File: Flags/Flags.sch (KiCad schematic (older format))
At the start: 22 parts, among them J1 Conn_01x07_Male, J2 Conn_01x06_Male, J3 Conn_01x03_Male, J4 Conn_01x04_Male, U1 74LS08, U2 74HC74, U3 74LS175

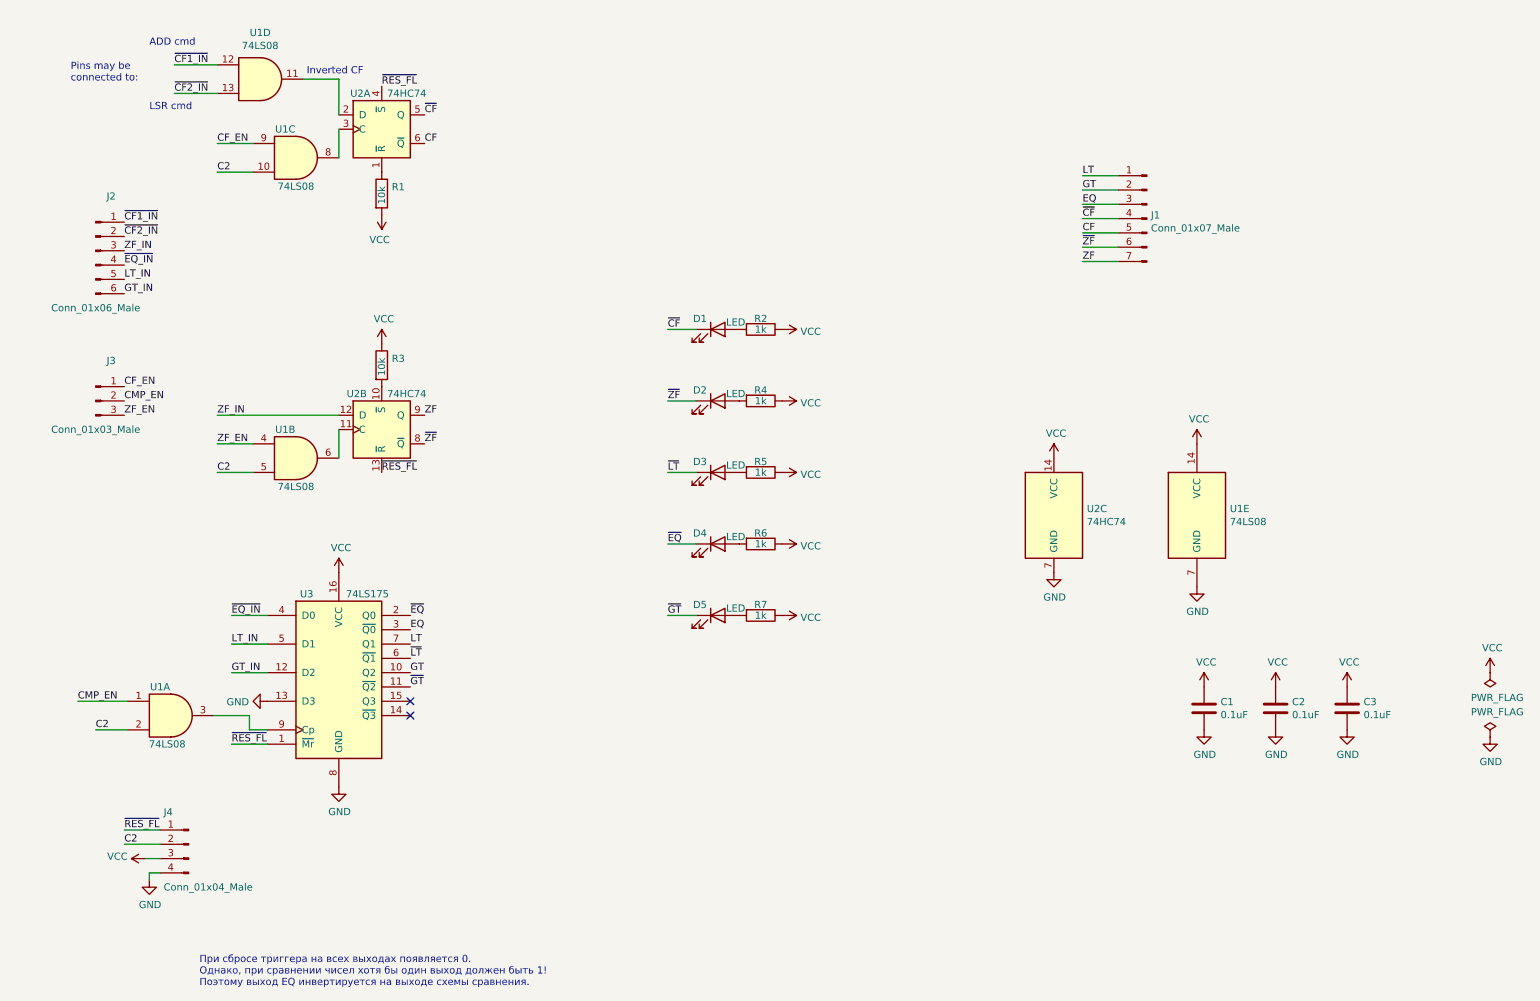
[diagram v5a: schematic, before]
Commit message: Polishing Flags. Add lost pins.
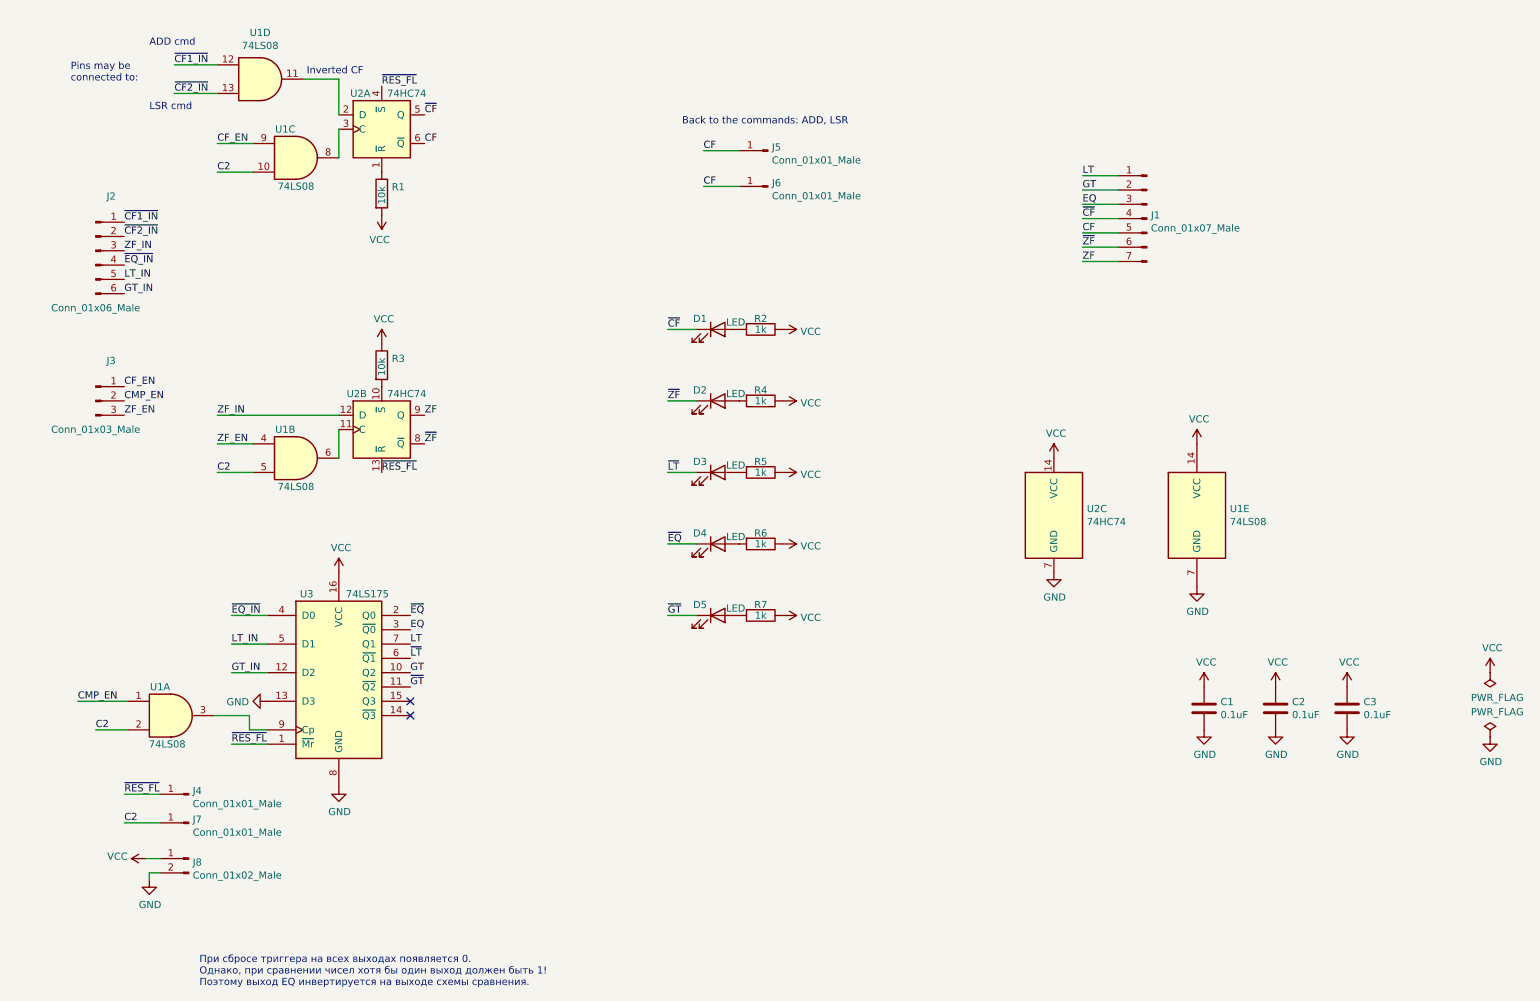
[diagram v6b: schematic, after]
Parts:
- removed J4: Conn_01x04_Male, Connector_PinHeader_2.54mm:PinHeader_1x04_P2.54mm_Vertical, symbol Connector:Conn_01x04_Male
- added J4, J5, J6, J7: Conn_01x01_Male, Connector_PinHeader_2.54mm:PinHeader_1x01_P2.54mm_Vertical, symbol Connector:Conn_01x01_Male
- added J8: Conn_01x02_Male, Connector_PinHeader_2.54mm:PinHeader_1x02_P2.54mm_Vertical, symbol Connector:Conn_01x02_Male
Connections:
- net C2: now also J7.1 (Pin_1)
- net CF: now also J5.1 (Pin_1), J6.1 (Pin_1)
- net GND: now also J8.2 (Pin_2)
- net VCC: now also J8.1 (Pin_1)
- net ~RES_FL: now also J4.1 (Pin_1)
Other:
- note added: "Back to the commands: ADD, LSR"
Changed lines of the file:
@@
 Text Label 7900 2525 0    50   ~ 0
 ZF
-$Comp
-L Connector:Conn_01x04_Male J4
-U 1 1 62C55960
-P 1650 6600
-F 0 "J4" H 1825 6825 50  0000 R CNN
-F 1 "Conn_01x04_Male" H 1825 6300 50  0000 R CNN
-F 2 "Connector_PinHeader_2.54mm:PinHeader_1x04_P2.54mm_Vertical" H 1650 6600 50  0001 C CNN
-F 3 "~" H 1650 6600 50  0001 C CNN
-	1    1650 6600
-	-1   0    0    -1
-$EndComp
-Wire Wire Line
-	1200 6500 1450 6500
-Wire Wire Line
-	1200 6600 1450 6600
-Text Label 1200 6600 0    50   ~ 0
+Wire Wire Line
+	1200 6250 1450 6250
+Wire Wire Line
+	1200 6450 1450 6450
+Text Label 1200 6450 0    50   ~ 0
 C2
-Text Label 1200 6500 0    50   ~ 0
+Text Label 1200 6250 0    50   ~ 0
 ~RES_FL
 $Comp
@@
 	-1   0    0    -1
 $EndComp
+$Comp
+L Connector:Conn_01x01_Male J5
+U 1 1 63FB964B
+P 5700 1750
+F 0 "J5" H 5672 1774 50  0000 R CNN
+F 1 "Conn_01x01_Male" H 5672 1683 50  0000 R CNN
+F 2 "Connector_PinHeader_2.54mm:PinHeader_1x01_P2.54mm_Vertical" H 5700 1750 50  0001 C CNN
+F 3 "~" H 5700 1750 50  0001 C CNN
+	1    5700 1750
+	-1   0    0    -1
+$EndComp
+$Comp
+L Connector:Conn_01x01_Male J6
+U 1 1 63FBB2B0
+P 5700 2000
+F 0 "J6" H 5672 2024 50  0000 R CNN
+F 1 "Conn_01x01_Male" H 5672 1933 50  0000 R CNN
+F 2 "Connector_PinHeader_2.54mm:PinHeader_1x01_P2.54mm_Vertical" H 5700 2000 50  0001 C CNN
+F 3 "~" H 5700 2000 50  0001 C CNN
+	1    5700 2000
+	-1   0    0    -1
+$EndComp
+Wire Wire Line
+	5250 1750 5500 1750
+Wire Wire Line
+	5250 2000 5500 2000
+Text Label 5250 1750 0    50   ~ 0
+CF
+Text Label 5250 2000 0    50   ~ 0
+CF
+Text Notes 5100 1575 0    50   ~ 0
+Back to the commands: ADD, LSR
+$Comp
+L Connector:Conn_01x02_Male J8
+U 1 1 640113A9
+P 1650 6700
+F 0 "J8" H 1622 6674 50  0000 R CNN
+F 1 "Conn_01x02_Male" H 1622 6583 50  0000 R CNN
+F 2 "Connector_PinHeader_2.54mm:PinHeader_1x02_P2.54mm_Vertical" H 1650 6700 50  0001 C CNN
+F 3 "~" H 1650 6700 50  0001 C CNN
+	1    1650 6700
+	-1   0    0    -1
+$EndComp
+$Comp
+L Connector:Conn_01x01_Male J4
+U 1 1 64013AFE
+P 1650 6250
+F 0 "J4" H 1622 6274 50  0000 R CNN
+F 1 "Conn_01x01_Male" H 1622 6183 50  0000 R CNN
+F 2 "Connector_PinHeader_2.54mm:PinHeader_1x01_P2.54mm_Vertical" H 1650 6250 50  0001 C CNN
+F 3 "~" H 1650 6250 50  0001 C CNN
+	1    1650 6250
+	-1   0    0    -1
+$EndComp
+$Comp
+L Connector:Conn_01x01_Male J7
+U 1 1 6401693F
+P 1650 6450
+F 0 "J7" H 1622 6474 50  0000 R CNN
+F 1 "Conn_01x01_Male" H 1622 6383 50  0000 R CNN
+F 2 "Connector_PinHeader_2.54mm:PinHeader_1x01_P2.54mm_Vertical" H 1650 6450 50  0001 C CNN
+F 3 "~" H 1650 6450 50  0001 C CNN
+	1    1650 6450
+	-1   0    0    -1
+$EndComp

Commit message: Polishing Flags. Add mounting holes.
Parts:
- added H1, H2: MountingHole, MountingHole:MountingHole_3.2mm_M3, symbol Mechanical:MountingHole
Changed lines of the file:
@@
 	-1   0    0    -1
 $EndComp
+$Comp
+L Mechanical:MountingHole H1
+U 1 1 64692F19
+P 7500 5500
+F 0 "H1" H 7600 5546 50  0000 L CNN
+F 1 "MountingHole" H 7600 5455 50  0000 L CNN
+F 2 "MountingHole:MountingHole_3.2mm_M3" H 7500 5500 50  0001 C CNN
+F 3 "~" H 7500 5500 50  0001 C CNN
+	1    7500 5500
+	1    0    0    -1
+$EndComp
+$Comp
+L Mechanical:MountingHole H2
+U 1 1 64693311
+P 7500 5750
+F 0 "H2" H 7600 5796 50  0000 L CNN
+F 1 "MountingHole" H 7600 5705 50  0000 L CNN
+F 2 "MountingHole:MountingHole_3.2mm_M3" H 7500 5750 50  0001 C CNN
+F 3 "~" H 7500 5750 50  0001 C CNN
+	1    7500 5750
+	1    0    0    -1
+$EndComp
 $EndSCHEMATC

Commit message: Polishing Flags
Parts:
- added H3, H4: MountingHole, MountingHole:MountingHole_3.2mm_M3, symbol Mechanical:MountingHole
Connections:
- net CMP_EN: now also J3.3 (Pin_3); no longer J3.2 (Pin_2)
- net ZF_EN: now also J3.2 (Pin_2); no longer J3.3 (Pin_3)
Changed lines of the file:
@@
 Text Label 1200 2450 0    50   ~ 0
 ZF_IN
+Text Label 1200 3500 0    50   ~ 0
+ZF_EN
 Text Label 1200 3600 0    50   ~ 0
-ZF_EN
-Text Label 1200 3500 0    50   ~ 0
 CMP_EN
 Text Label 1200 2650 0    50   ~ 0
@@
 	1    0    0    -1
 $EndComp
+$Comp
+L Mechanical:MountingHole H3
+U 1 1 6469DB14
+P 7500 6000
+F 0 "H3" H 7600 6046 50  0000 L CNN
+F 1 "MountingHole" H 7600 5955 50  0000 L CNN
+F 2 "MountingHole:MountingHole_3.2mm_M3" H 7500 6000 50  0001 C CNN
+F 3 "~" H 7500 6000 50  0001 C CNN
+	1    7500 6000
+	1    0    0    -1
+$EndComp
+$Comp
+L Mechanical:MountingHole H4
+U 1 1 646C277F
+P 7500 6250
+F 0 "H4" H 7600 6296 50  0000 L CNN
+F 1 "MountingHole" H 7600 6205 50  0000 L CNN
+F 2 "MountingHole:MountingHole_3.2mm_M3" H 7500 6250 50  0001 C CNN
+F 3 "~" H 7500 6250 50  0001 C CNN
+	1    7500 6250
+	1    0    0    -1
+$EndComp
